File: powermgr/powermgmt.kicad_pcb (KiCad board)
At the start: 2 copper layers, 83.8 x 40.1 mm, 22 parts, among them IC1 74HC4094_RevA_23Aug2012, IC2 AP24x1, IC3 AP24x1, IC4 AP24x1, IC5 AP24x1, IC6 AP24x1, IC7 AP24x1, IC8 AP24x1, IC9 AP24x1, J1 CONN_01X06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

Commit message: add LEDs and pulldowns
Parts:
- added C1: 100n, Capacitors_SMD:C_0805_HandSoldering, F.Cu at (65.8, 64.5)
- added C10: 100n, Capacitors_SMD:C_0805_HandSoldering, F.Cu at (65.2, 19.4)
- added C11: 100n, Capacitors_SMD:C_0805_HandSoldering, F.Cu at (67.1, 65.8)
- added C12: 100n, Capacitors_SMD:C_0805_HandSoldering, F.Cu at (35.3, 16.3)
- added C2: 100n, Capacitors_SMD:C_0805_HandSoldering, F.Cu at (42.3, 16.9)
- added C3: 100n, Capacitors_SMD:C_0805_HandSoldering, F.Cu at (60.7, 74.7)
- added C4: 100n, Capacitors_SMD:C_0805_HandSoldering, F.Cu at (31.5, 82.3)
- added C5: 100n, Capacitors_SMD:C_0805_HandSoldering, F.Cu at (54.4, 81.0)
- added C6: 100n, Capacitors_SMD:C_0805_HandSoldering, F.Cu at (51.8, 72.1)
- added C7: 100n, Capacitors_SMD:C_0805_HandSoldering, F.Cu at (37.8, 27.1)
- added C8: 100n, Capacitors_SMD:C_0805_HandSoldering, F.Cu at (86.1, 22.6)
- added C9: 100n, Capacitors_SMD:C_0805_HandSoldering, F.Cu at (46.7, 17.5)
- added D10: LED_Small, LEDs:LED_0805, F.Cu at (18.2, 69.6)
- added D3: LED_Small, LEDs:LED_0805, F.Cu at (86.1, 43.4)
- added D4: LED_Small, LEDs:LED_0805, F.Cu at (74.7, 65.8)
- added D5: LED_Small, LEDs:LED_0805, F.Cu at (82.3, 65.8)
- added D6: LED_Small, LEDs:LED_0805, F.Cu at (25.8, 64.5)
- added D7: LED_Small, LEDs:LED_0805, F.Cu at (48.0, 62.0)
- added D8: LED_Small, LEDs:LED_0805, F.Cu at (56.9, 60.7)
- added D9: LED_Small, LEDs:LED_0805, F.Cu at (72.1, 62.0)
- added R10: 100k, Resistors_SMD:R_0805_HandSoldering, F.Cu at (86.4, 31.8)
- added R11: 100k, Resistors_SMD:R_0805_HandSoldering, F.Cu at (79.5, 31.8)
- added R12: 100k, Resistors_SMD:R_0805_HandSoldering, F.Cu at (72.4, 31.8)
- added R13: 100k, Resistors_SMD:R_0805_HandSoldering, F.Cu at (65.3, 31.8)
- added R14: 100k, Resistors_SMD:R_0805_HandSoldering, F.Cu at (58.2, 31.8)
- added R15: 100k, Resistors_SMD:R_0805_HandSoldering, F.Cu at (51.3, 31.8)
- added R16: 100k, Resistors_SMD:R_0805_HandSoldering, F.Cu at (44.2, 31.8)
- added R17: 100k, Resistors_SMD:R_0805_HandSoldering, F.Cu at (37.3, 31.8)
- added R2: 4k7, Resistors_SMD:R_0805_HandSoldering, F.Cu at (88.4, 42.9)
- added R3: 4k7, Resistors_SMD:R_0805_HandSoldering, F.Cu at (29.0, 75.9)
- added R4: 4k7, Resistors_SMD:R_0805_HandSoldering, F.Cu at (44.2, 78.5)
- added R5: 4k7, Resistors_SMD:R_0805_HandSoldering, F.Cu at (19.4, 65.2)
- added R6: 4k7, Resistors_SMD:R_0805_HandSoldering, F.Cu at (37.8, 79.8)
- added R7: 4k7, Resistors_SMD:R_0805_HandSoldering, F.Cu at (46.7, 87.4)
- added R8: 4k7, Resistors_SMD:R_0805_HandSoldering, F.Cu at (25.1, 19.4)
- added R9: 4k7, Resistors_SMD:R_0805_HandSoldering, F.Cu at (82.3, 82.3)
- moved R1 37.6 mm to (114.3, 24.6)
- moved D2 27.0 mm to (112.0, 38.1)
- moved D1 26.6 mm to (112.5, 32.5)
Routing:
- net GND: track 340.2 -> 266.4 mm
- net OVERLOAD: track 73.6 -> 0.00 mm, vias 2 -> 0
- net ctrl_out7: track 27.2 -> 0.00 mm, vias 2 -> 0
- net ctrl_out6: track 20.9 -> 0.00 mm, vias 4 -> 0
- net ctrl_out5: track 15.2 -> 0.00 mm, vias 4 -> 0
- net ctrl_out4: track 11.2 -> 0.05 mm, vias 2 -> 0
- net Net-(D1-Pad1): track 10.4 -> 0.00 mm
- net VPWR: track 185.0 -> 175.9 mm
- net ctrl_out1: track 23.6 -> 21.9 mm, vias 2 -> 1
- net ctrl_out0: track 30.1 -> 28.7 mm, vias 2 -> 1
- net ctrl_out3: vias 2 -> 1
- net ctrl_out2: vias 2 -> 1

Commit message: almost done
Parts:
- moved C4 85.2 mm to (109.5, 47.9)
- moved R9 68.1 mm to (26.7, 43.1), turned to 90 degrees
- moved R5 66.4 mm to (82.0, 43.1), turned to 90 degrees
- moved R3 66.4 mm to (86.6, 43.1), turned to 90 degrees
- moved C2 66.1 mm to (104.9, 38.0)
- moved C3 65.3 mm to (106.4, 28.1)
- moved D6 58.7 mm to (82.0, 47.6), turned to 270 degrees
- moved C5 55.5 mm to (66.0, 26.8)
- moved R4 53.5 mm to (84.3, 43.1), turned to 90 degrees
- moved C1 51.4 mm to (105.9, 32.4)
- moved R7 47.0 mm to (31.2, 43.1), turned to 90 degrees
- moved D9 45.5 mm to (29.0, 47.6), turned to 270 degrees
- moved C6 45.3 mm to (51.8, 26.8)
- moved C11 44.8 mm to (45.0, 26.8)
- moved R6 37.0 mm to (33.5, 43.1), turned to 90 degrees
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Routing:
- net GND: track 266.4 -> 689.8 mm, vias 0 -> 111
- net OVERLOAD: track 0.00 -> 59.9 mm, vias 0 -> 8
- net (no net): track 0.00 -> 44.7 mm, vias 0 -> 32
- net ctrl_out7: track 0.00 -> 40.1 mm, vias 0 -> 2
- net ctrl_out4: track 0.05 -> 39.8 mm, vias 0 -> 3
- net ctrl_out6: track 0.00 -> 38.3 mm, vias 0 -> 2
- net ctrl_out5: track 0.00 -> 36.9 mm, vias 0 -> 2
- net ctrl_out3: track 9.66 -> 30.8 mm, vias 1 -> 2
- net Net-(D1-Pad1): track 0.00 -> 19.8 mm, vias 0 -> 2
- net ctrl_out2: track 16.0 -> 34.9 mm, vias 1 -> 3
- net ctrl_out1: track 21.9 -> 38.7 mm, vias 1 -> 3
- net VPWR: track 175.9 -> 189.3 mm
- net ctrl_out0: track 28.7 -> 41.6 mm, vias 1 -> 3
- net /Power out/out_pwr6: track 8.37 -> 10.5 mm
- net /Power out/out_pwr7: track 8.50 -> 10.6 mm
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
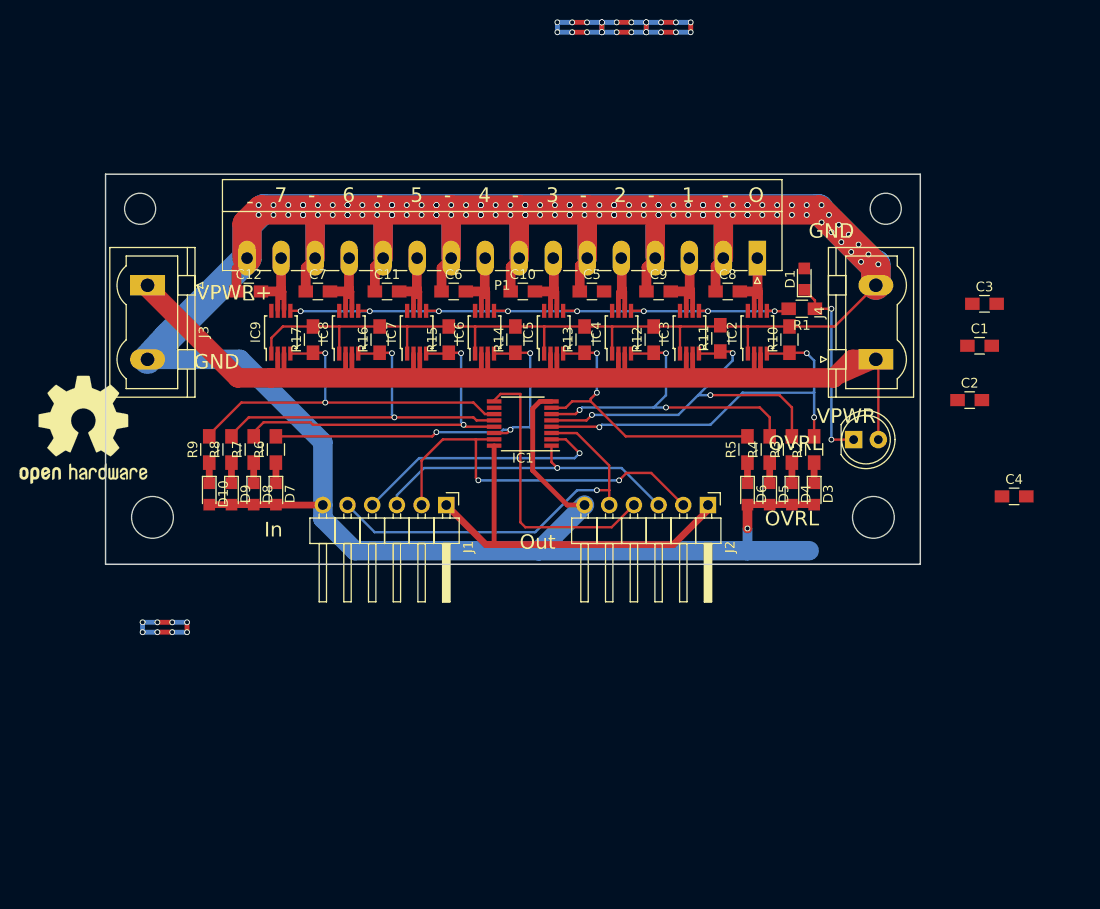
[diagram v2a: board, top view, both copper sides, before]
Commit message: copper filling, thicker power tracks
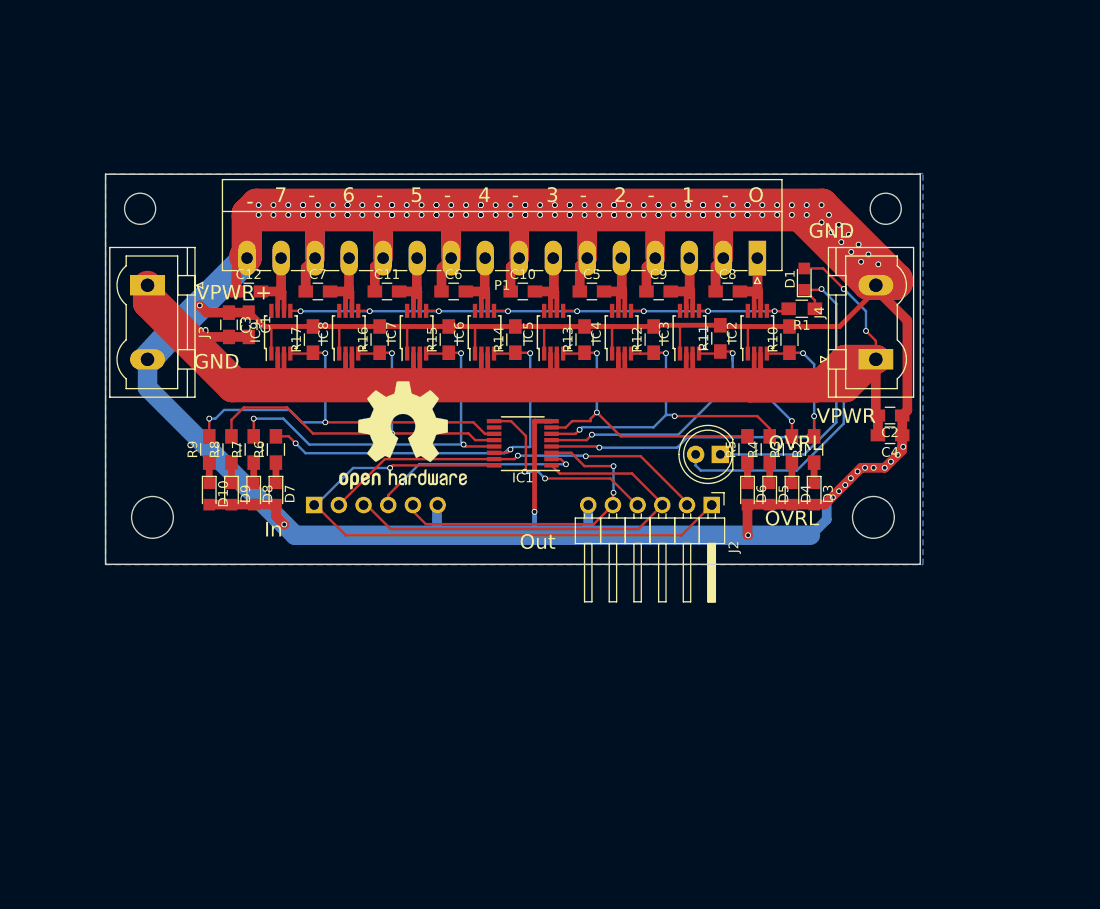
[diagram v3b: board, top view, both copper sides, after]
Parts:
- J1: moved to B.Cu
- moved C3 77.8 mm to (28.7, 30.2), turned to 270 degrees
- moved C1 75.2 mm to (30.7, 30.2), turned to 270 degrees
- moved REF*** 32.9 mm to (46.6, 41.6)
- moved C4 14.2 mm to (96.7, 41.6), turned to 180 degrees
- moved D2 13.8 mm to (79.2, 43.6), turned to 180 degrees
- moved J1 13.6 mm to (37.5, 48.8)
- moved C2 8.34 mm to (96.7, 39.6), turned to 180 degrees
- moved IC1 2.03 mm to (58.9, 42.4)
- moved J2 0.38 mm to (78.4, 48.8)
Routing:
- net GND: track 689.8 -> 881.1 mm, vias 111 -> 125
- net VPWR: track 189.3 -> 331.0 mm, vias 0 -> 2
- net (no net): track 44.7 -> 0.00 mm, vias 32 -> 0
- net VCC: track 40.9 -> 63.7 mm, vias 0 -> 1
- net Net-(IC1-Pad1): track 33.2 -> 45.9 mm, vias 1 -> 0
- net Net-(D1-Pad1): track 19.8 -> 31.9 mm, vias 2 -> 1
- net Net-(IC1-Pad9): track 29.1 -> 21.0 mm, vias 0 -> 2
- net Net-(IC1-Pad3): track 41.3 -> 34.3 mm, vias 1 -> 2
- net Net-(IC1-Pad2): track 27.0 -> 22.3 mm, vias 1 -> 2
- net ctrl_out5: track 36.9 -> 41.3 mm, vias 2 -> 3
- net ctrl_out6: track 38.3 -> 42.6 mm
- net ctrl_out7: track 40.1 -> 43.5 mm, vias 2 -> 3
- net ctrl_out4: track 39.8 -> 42.4 mm
- net /Power out/out_pwr2: track 8.37 -> 10.2 mm
- net ctrl_out3: track 30.8 -> 31.7 mm
- added copper zone on B.Cu, net GND
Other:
- board text removed: "Limits: 2A per output (2.1-2.5 current limit), 16A total OVRL will lit if any of outputs is in error state Outputs will have ~200 ohm resistance when off (capacitor discharge functionality) Out port is used for chaining modules"
